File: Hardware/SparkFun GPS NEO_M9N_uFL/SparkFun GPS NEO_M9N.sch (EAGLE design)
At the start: 51 parts, among them J13 U.FL, J2 Qwiic Right Angle, J4 Qwiic Right Angle, U1 U-BLOX_NEO-M9N, U2 3.3V

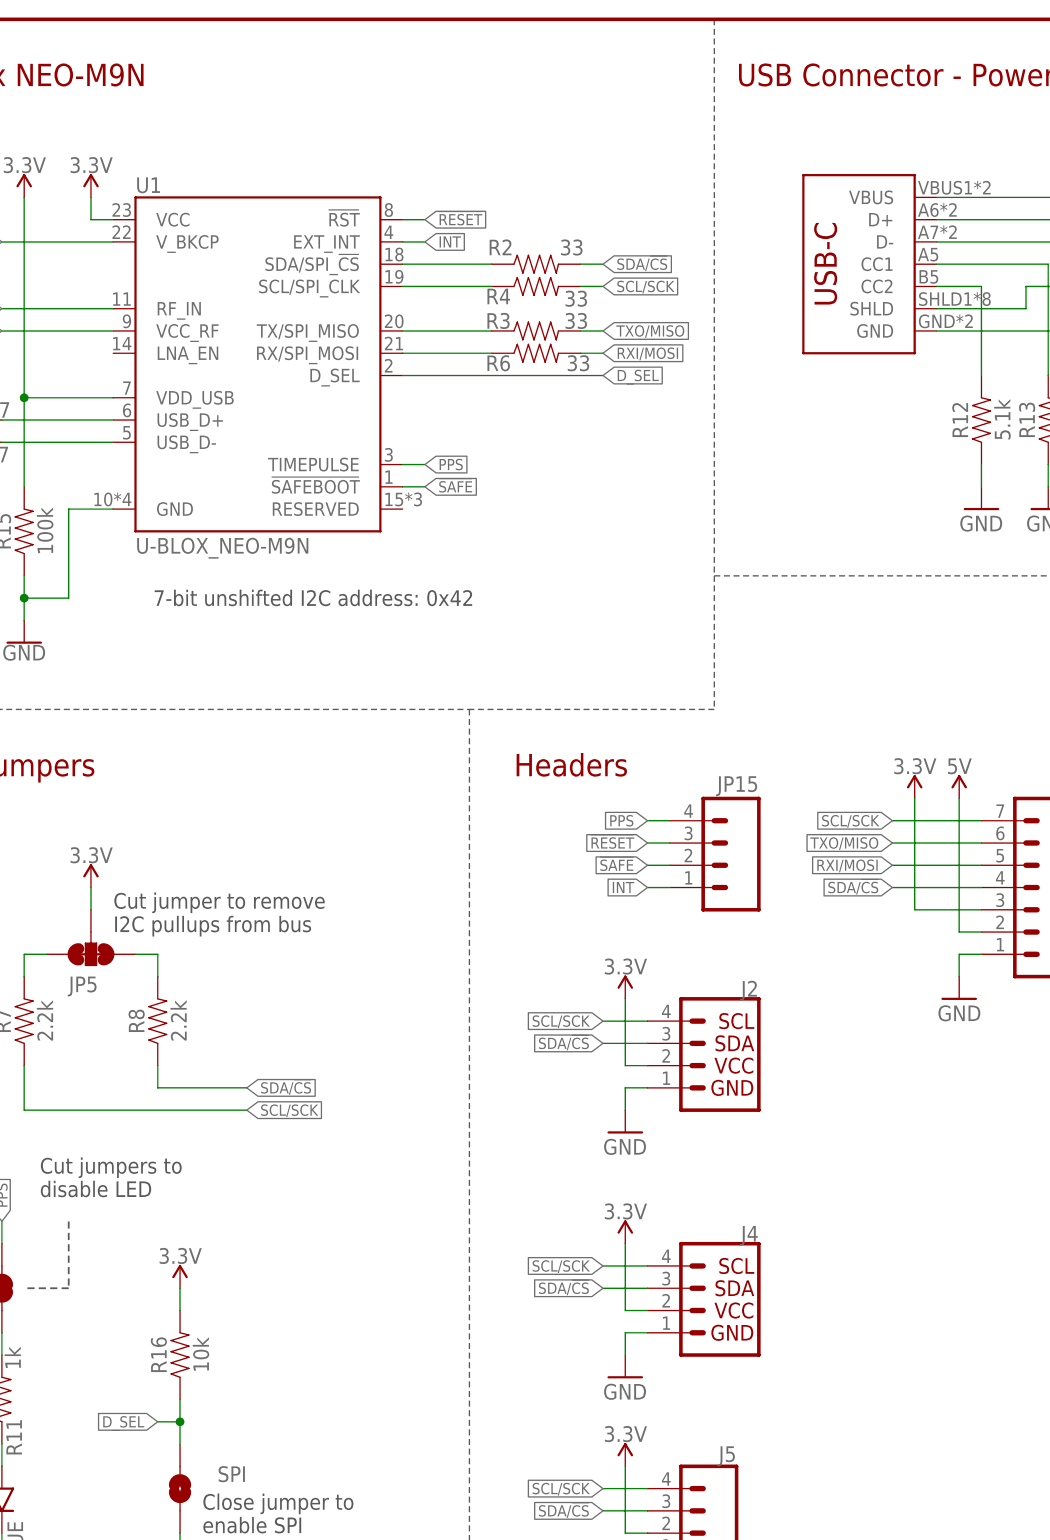
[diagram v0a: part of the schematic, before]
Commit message: Fixes small DRC problems, Adds silk to battery, adds production id to NEO-M9N chip
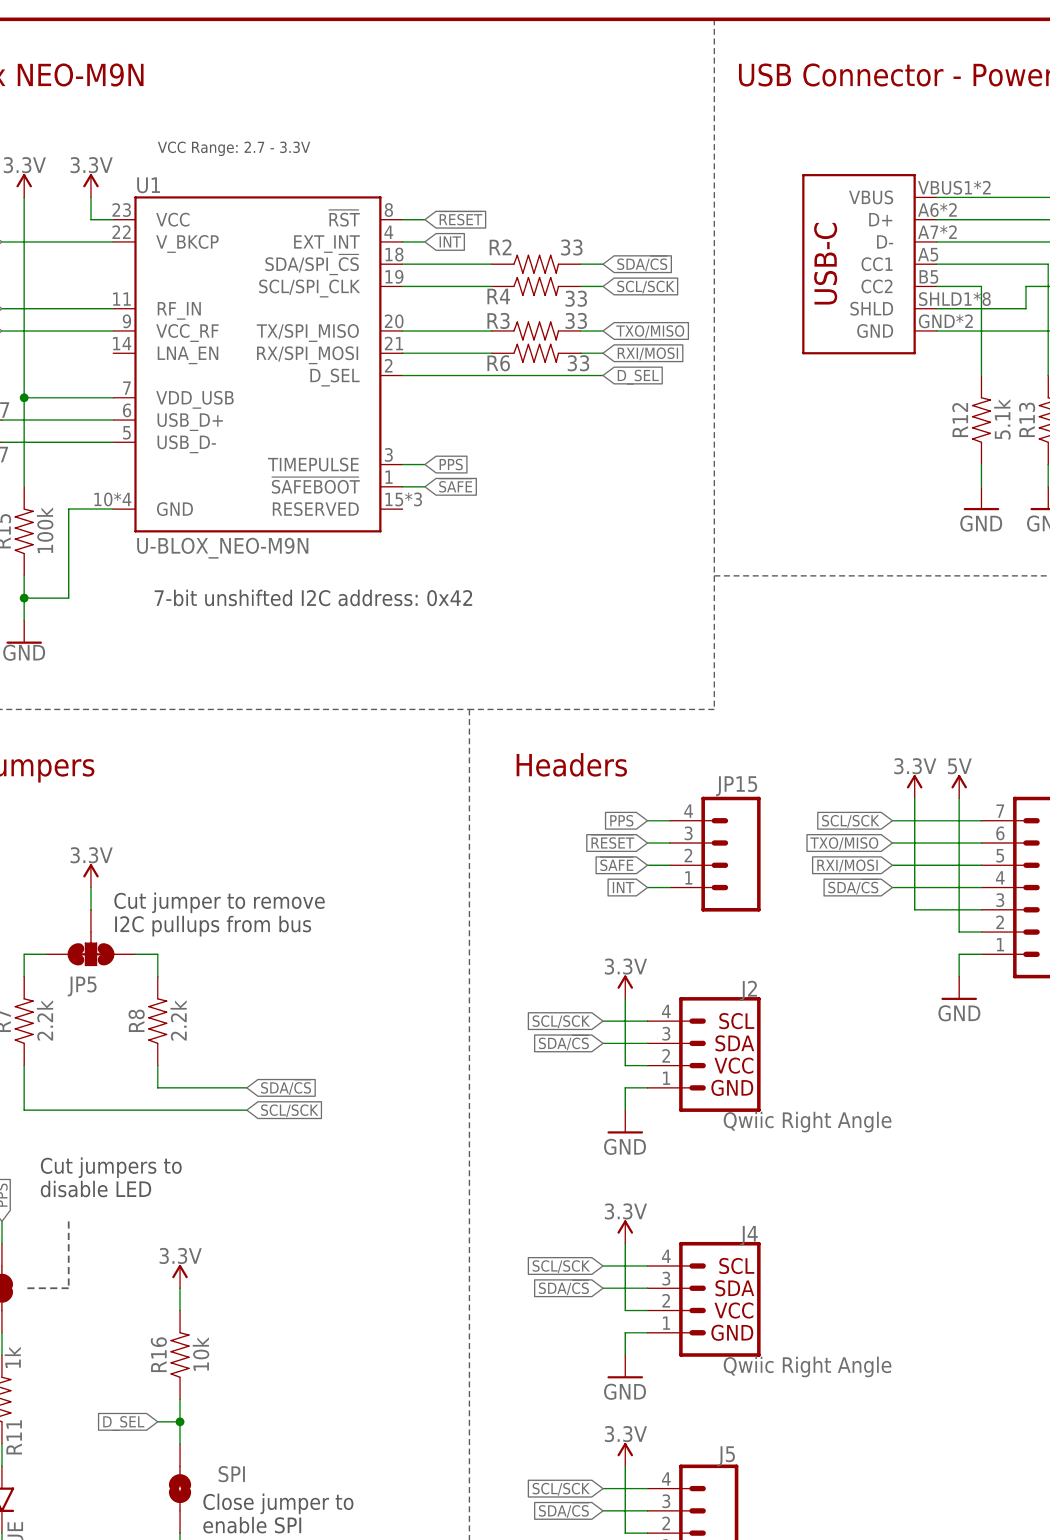
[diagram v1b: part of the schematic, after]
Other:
- note added: "VCC Range: 2.7 - 3.3V"
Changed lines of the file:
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@@
 <text x="104.14" y="177.8" size="2.54" layer="94" font="vector">USB Connector - Power</text>
 <text x="148.844" y="6.604" size="2.54" layer="94" font="vector">Based on design by: Nathan Seidle</text>
+<text x="38.1" y="170.18" size="1.27" layer="97" font="vector">VCC Range: 2.7 - 3.3V</text>
 </plain>
 <instances>
@@
 </instance>
 <instance part="J2" gate="G$1" x="101.6" y="66.04" smashed="yes" rot="MR0">
+<attribute name="VALUE" x="121.92" y="60.706" size="1.778" layer="96" font="vector" rot="MR0" align="top-left"/>
 <attribute name="NAME" x="106.68" y="73.914" size="1.778" layer="95" font="vector" rot="MR0"/>
 </instance>
@@
 </instance>
 <instance part="J4" gate="G$1" x="101.6" y="38.1" smashed="yes" rot="MR0">
+<attribute name="VALUE" x="121.92" y="32.766" size="1.778" layer="96" font="vector" rot="MR0" align="top-left"/>
 <attribute name="NAME" x="106.68" y="45.974" size="1.778" layer="95" font="vector" rot="MR0"/>
 </instance>
